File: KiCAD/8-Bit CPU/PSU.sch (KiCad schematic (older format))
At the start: 5 parts, among them J5 7-20V, U48 K7805M-1000R3

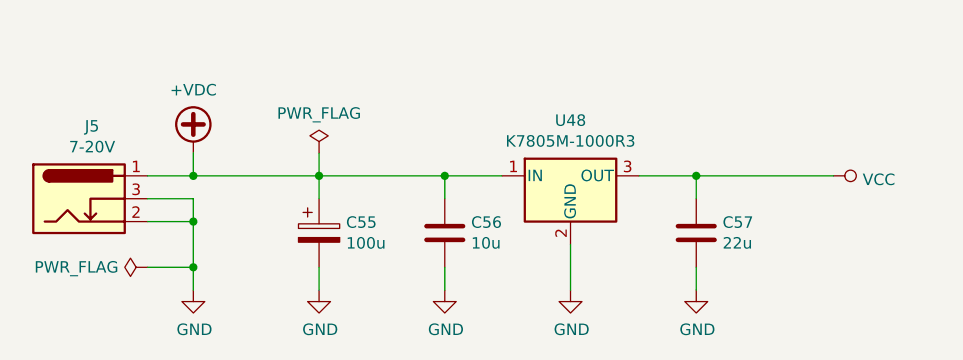
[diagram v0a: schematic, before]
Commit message: KiCAD cleanup - Revision A
Revision A Known Issues:
 * ATTiny45 has incorrect footprint
 * Flags register is redundant (The ATMega16's output port is a register)
 * Power jack pinout is wrong (12V shorted to ground)
 * Step counter reset logic is wrong (Active high signalling, Active low input)
 * ALU output indicator not connected
 * HLT indicator missing
 * EEPROMs can't be page written due to addressing setup (minor annoyance)
 * Flags Logic uses NAND gates instead of AND (fixed on the board I built)
 * Programmer needs to be able to toggle EEPROM outputs and Addressing Devices
    with different signals to enable reading.
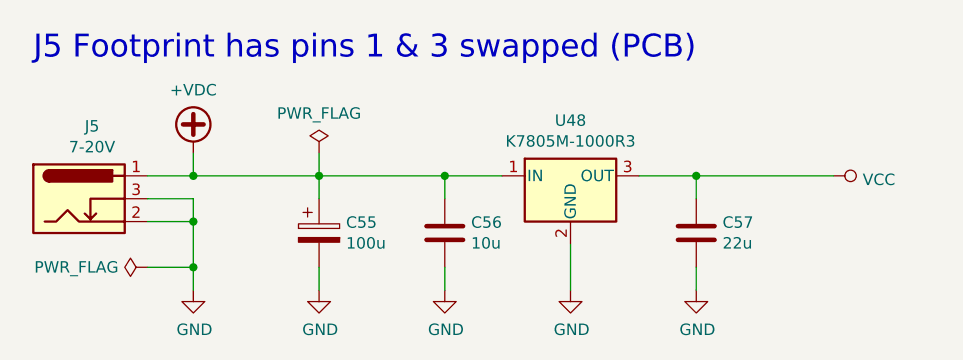
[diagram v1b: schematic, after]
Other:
- note added: "J5 Footprint has pins 1 & 3 swapped (PCB)"
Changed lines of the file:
@@
 $Descr A4 11693 8268
 encoding utf-8
-Sheet 28 30
+Sheet 28 29
 Title ""
 Date ""
@@
 Wire Wire Line
 	6400 3500 7000 3500
+Text Notes 3500 3000 0    100  ~ 0
+J5 Footprint has pins 1 & 3 swapped (PCB)
 $EndSCHEMATC

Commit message: KiCAD files update & Gerbers
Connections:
- net labels added: +12V
- net labels removed: +VDC
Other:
- note removed: "J5 Footprint has pins 1 & 3 swapped (PCB)"
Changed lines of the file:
@@
 $Descr A4 11693 8268
 encoding utf-8
-Sheet 28 29
+Sheet 27 29
 Title ""
 Date ""
-Rev ""
+Rev "C"
 Comp ""
 Comment1 ""
@@
 	1    0    0    -1
 $EndComp
-$Comp
-L power:+VDC #PWR0268
-U 1 1 5D5D1AE9
-P 4200 3400
-F 0 "#PWR0268" H 4200 3300 50  0001 C CNN
-F 1 "+VDC" H 4200 3675 50  0000 C CNN
-F 2 "" H 4200 3400 50  0001 C CNN
-F 3 "" H 4200 3400 50  0001 C CNN
-	1    4200 3400
-	1    0    0    -1
-$EndComp
-Wire Wire Line
-	4000 3500 4200 3500
-Wire Wire Line
-	4200 3500 4200 3400
 Wire Wire Line
 	4000 3600 4200 3600
@@
 	4200 3700 4200 3900
 $Comp
-L power:GND #PWR0269
+L power:GND #PWR0266
 U 1 1 5D5D1AF6
 P 4200 4000
-F 0 "#PWR0269" H 4200 3750 50  0001 C CNN
+F 0 "#PWR0266" H 4200 3750 50  0001 C CNN
 F 1 "GND" H 4205 3827 50  0000 C CNN
 F 2 "" H 4200 4000 50  0001 C CNN
@@
 $EndComp
 $Comp
-L power:GND #PWR0271
+L power:GND #PWR0268
 U 1 1 5D5D39D1
 P 5300 4000
-F 0 "#PWR0271" H 5300 3750 50  0001 C CNN
+F 0 "#PWR0268" H 5300 3750 50  0001 C CNN
 F 1 "GND" H 5305 3827 50  0000 C CNN
 F 2 "" H 5300 4000 50  0001 C CNN
@@
 $EndComp
 $Comp
-L power:GND #PWR0273
+L power:GND #PWR0270
 U 1 1 5D5D69A3
 P 6400 4000
-F 0 "#PWR0273" H 6400 3750 50  0001 C CNN
+F 0 "#PWR0270" H 6400 3750 50  0001 C CNN
 F 1 "GND" H 6405 3827 50  0000 C CNN
 F 2 "" H 6400 4000 50  0001 C CNN
@@
 $EndComp
 $Comp
-L power:GND #PWR0272
+L power:GND #PWR0269
 U 1 1 5D5D6E10
 P 5850 4000
-F 0 "#PWR0272" H 5850 3750 50  0001 C CNN
+F 0 "#PWR0269" H 5850 3750 50  0001 C CNN
 F 1 "GND" H 5855 3827 50  0000 C CNN
 F 2 "" H 5850 4000 50  0001 C CNN
@@
 	1    0    0    -1
 $EndComp
-Wire Wire Line
-	4200 3500 4750 3500
-Connection ~ 4200 3500
 Wire Wire Line
 	5300 3600 5300 3500
@@
 $EndComp
 $Comp
-L power:GND #PWR0270
+L power:GND #PWR0267
 U 1 1 5D5DCB5D
 P 4750 4000
-F 0 "#PWR0270" H 4750 3750 50  0001 C CNN
+F 0 "#PWR0267" H 4750 3750 50  0001 C CNN
 F 1 "GND" H 4755 3827 50  0000 C CNN
 F 2 "" H 4750 4000 50  0001 C CNN
@@
 Connection ~ 6400 3500
 $Comp
-L power:VCC #PWR0274
+L power:VCC #PWR0265
 U 1 1 5D5DD6D6
 P 7000 3500
-F 0 "#PWR0274" H 7000 3350 50  0001 C CNN
+F 0 "#PWR0265" H 7000 3350 50  0001 C CNN
 F 1 "VCC" V 7017 3628 50  0000 L CNN
 F 2 "" H 7000 3500 50  0001 C CNN
@@
 $EndComp
 $Comp
-L power:PWR_FLAG #FLG02
+L power:PWR_FLAG #FLG01
 U 1 1 5D5BC0AA
 P 4750 3400
-F 0 "#FLG02" H 4750 3475 50  0001 C CNN
+F 0 "#FLG01" H 4750 3475 50  0001 C CNN
 F 1 "PWR_FLAG" H 4750 3573 50  0000 C CNN
 F 2 "" H 4750 3400 50  0001 C CNN
@@
 $EndComp
 $Comp
-L power:PWR_FLAG #FLG01
+L power:PWR_FLAG #FLG02
 U 1 1 5D5BC868
 P 4000 3900
-F 0 "#FLG01" H 4000 3975 50  0001 C CNN
+F 0 "#FLG02" H 4000 3975 50  0001 C CNN
 F 1 "PWR_FLAG" V 4000 4027 50  0000 L CNN
 F 2 "" H 4000 3900 50  0001 C CNN
@@
 Wire Wire Line
 	6400 3500 7000 3500
-Text Notes 3500 3000 0    100  ~ 0
-J5 Footprint has pins 1 & 3 swapped (PCB)
+Wire Wire Line
+	4000 3500 4200 3500
+$Comp
+L power:+12V #PWR0264
+U 1 1 5DCFC781
+P 4200 3400
+F 0 "#PWR0264" H 4200 3250 50  0001 C CNN
+F 1 "+12V" H 4215 3573 50  0000 C CNN
+F 2 "" H 4200 3400 50  0001 C CNN
+F 3 "" H 4200 3400 50  0001 C CNN
+	1    4200 3400
+	1    0    0    -1
+$EndComp
+Wire Wire Line
+	4200 3400 4200 3500
+Connection ~ 4200 3500
+Wire Wire Line
+	4200 3500 4750 3500
 $EndSCHEMATC
